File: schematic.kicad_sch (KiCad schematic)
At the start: 15 parts, among them U1 MCP6001-OT

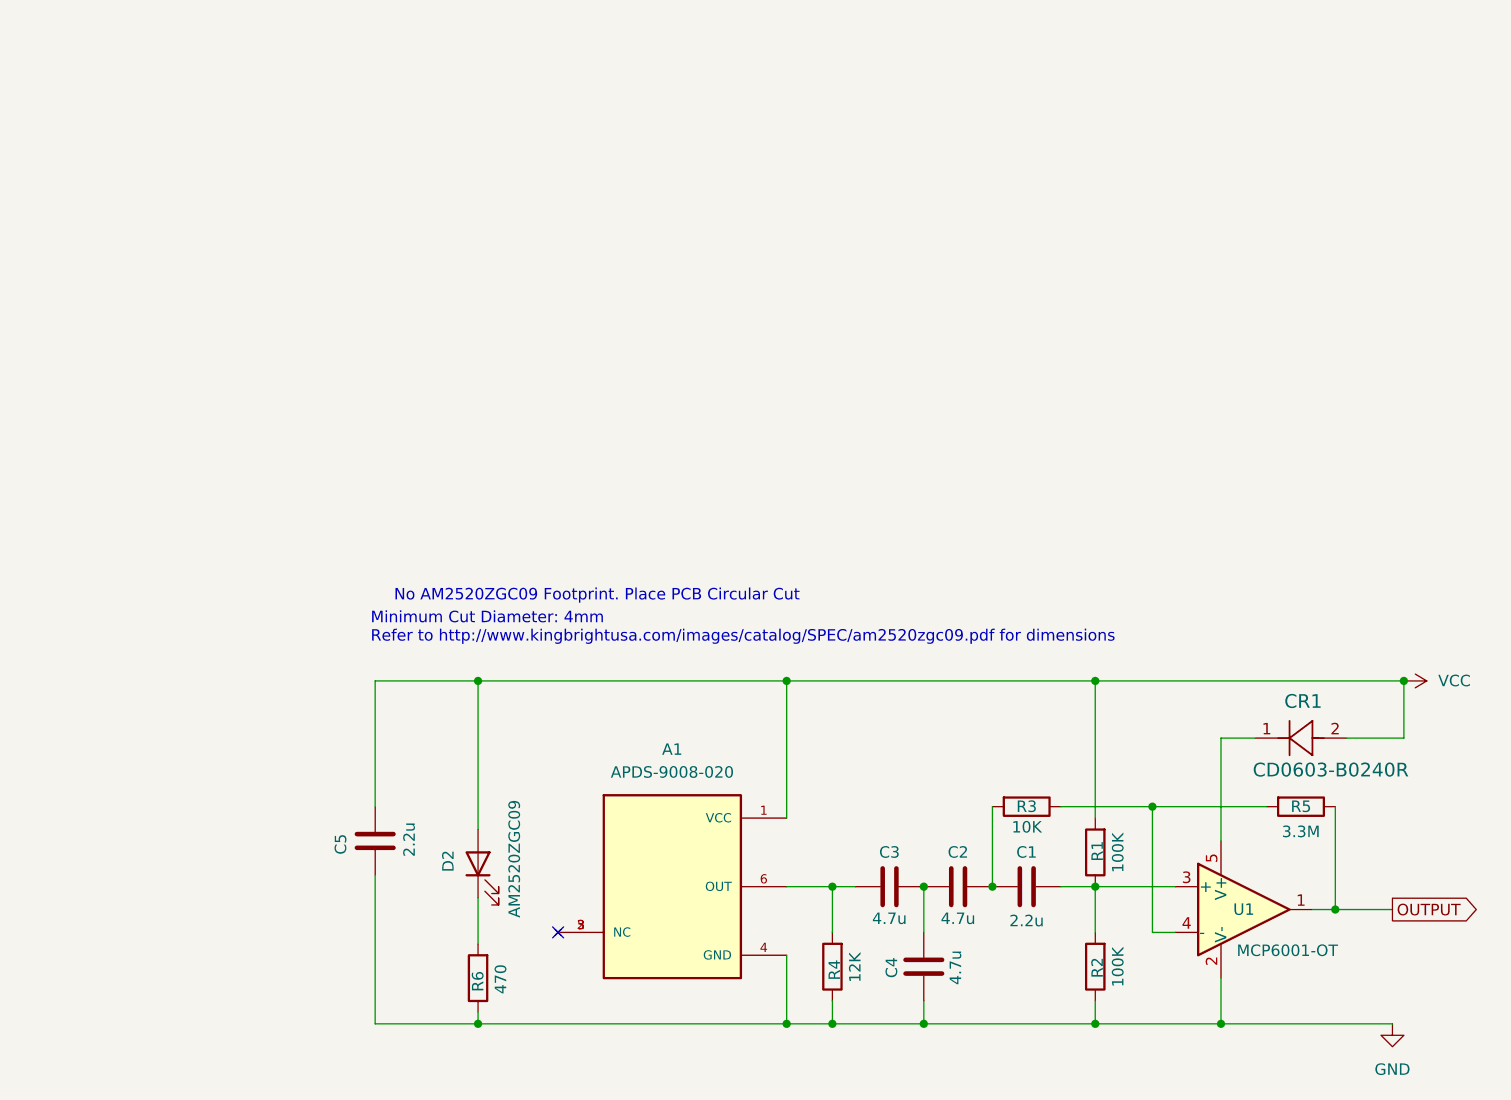
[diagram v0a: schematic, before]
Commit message: update the layout and the schematic
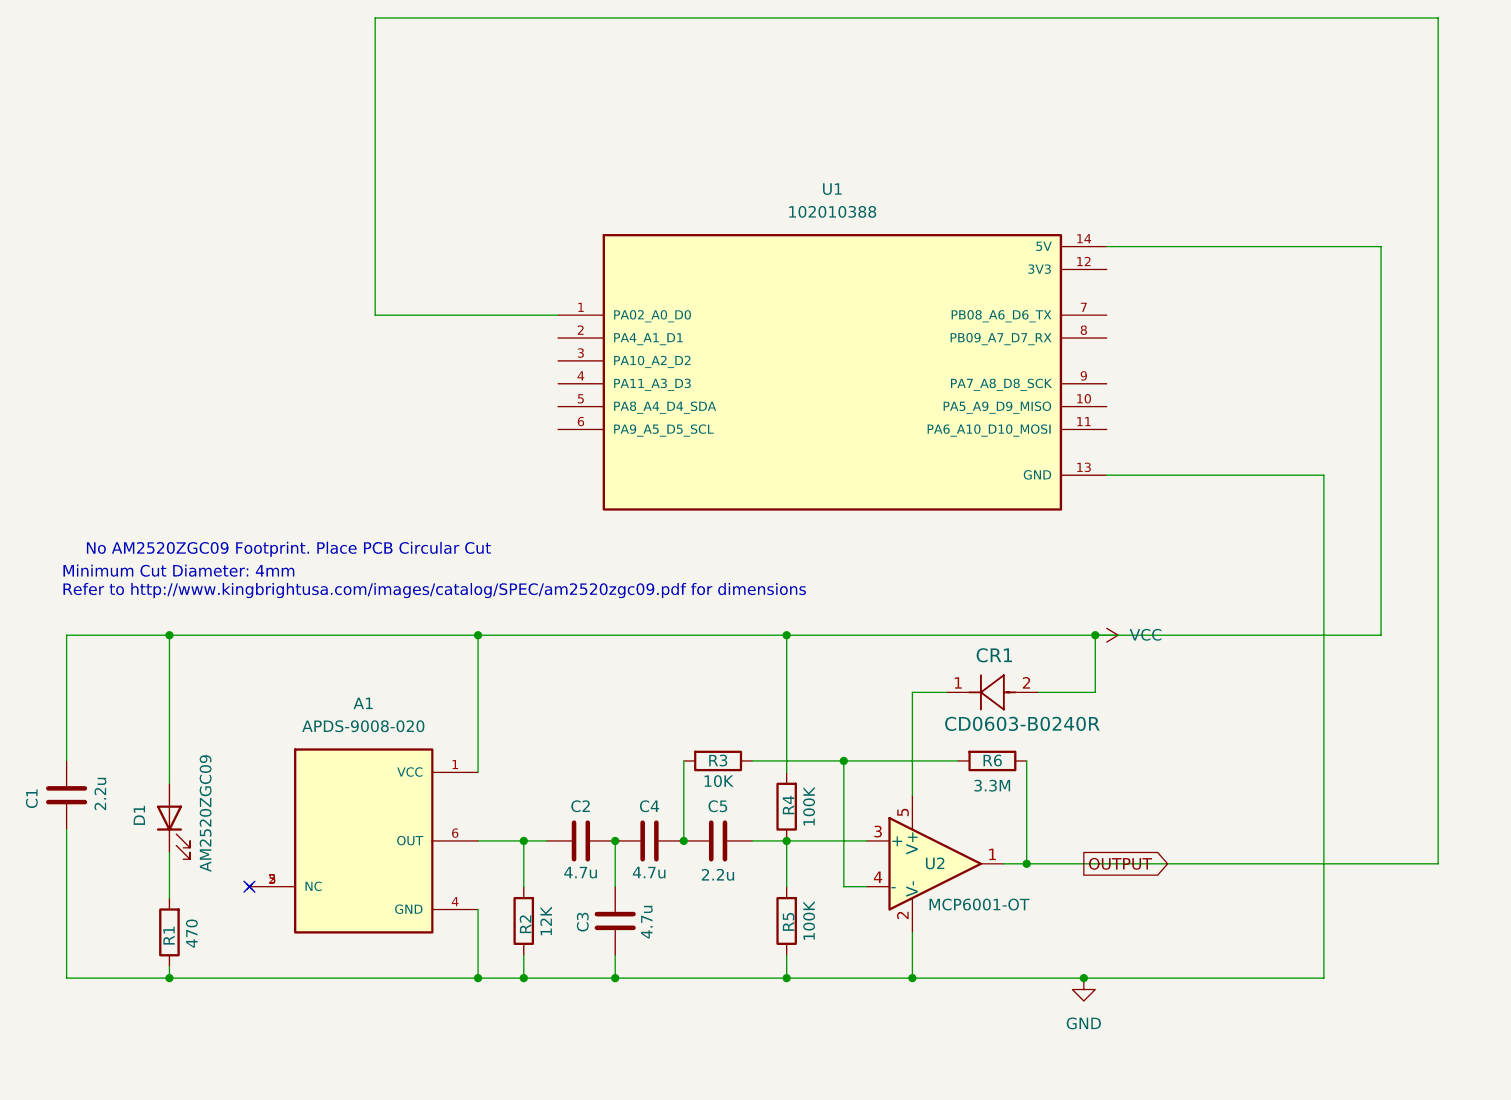
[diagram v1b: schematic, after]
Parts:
- removed D2: AM2520ZGC09, symbol Device:LED
- removed U1: MCP6001-OT, Package_TO_SOT_SMD:SOT-23-5, symbol Amplifier_Operational:MCP6001-OT
- added D1: AM2520ZGC09, LED_SMD:LED_0201_0603Metric, symbol Device:LED
- added U1: 102010388, 102010388:MODULE_102010388, symbol 102010388:102010388
- added U2: MCP6001-OT, Package_TO_SOT_SMD:HVSOF6, symbol Amplifier_Operational:MCP6001-OT
- A1: footprint (none) -> APDS-9008-020:XDCR_APDS-9008-020
- C1, C2, C3, C4, C5: footprint (none) -> Capacitor_SMD:C_0201_0603Metric_Pad0.64x0.40mm_HandSolder
- CR1: footprint DIODE_CD0603-B0240R_BRN -> footprints:DIODE_CD0603-B0240R_BRN
- R1: value 100K -> 470; footprint (none) -> Resistor_SMD:R_0201_0603Metric_Pad0.64x0.40mm_HandSolder
- R2: value 100K -> 12K; footprint (none) -> Resistor_SMD:R_0201_0603Metric_Pad0.64x0.40mm_HandSolder
- R3: footprint (none) -> Resistor_SMD:R_0201_0603Metric_Pad0.64x0.40mm_HandSolder
- R4: value 12K -> 100K; footprint (none) -> Resistor_SMD:R_0201_0603Metric_Pad0.64x0.40mm_HandSolder
- R5: value 3.3M -> 100K; footprint (none) -> Resistor_SMD:R_0201_0603Metric_Pad0.64x0.40mm_HandSolder
- R6: value 470 -> 3.3M; footprint (none) -> Resistor_SMD:R_0201_0603Metric_Pad0.64x0.40mm_HandSolder
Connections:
- net GND: now also C1.1, C3.2, R1.1, R5.1, U1.13 (GND), U2.2 (V-); no longer C4.2, C5.1, R4.1, R6.1
- net OUTPUT: now also R6.1, U1.1 (PA02_A0_D0), U2.1; no longer R5.1
- net VCC: now also C1.2, R4.2, D1.2 (A), U1.14 (5V); no longer C5.2, R1.2
- net at R5.2: now also C5.2, R4.1, U2.3 (+); no longer R3.1
- net at CR1.1: now also U2.5 (V+)
- net at R6.2: now also R3.1, U2.4 (-)
- new net: A1.6 (OUT), C2.1, R2.2
- new net: C2.2, C3.1, C4.1
- new net: D1.1 (K), R1.2
- new net: C4.2, C5.1, R3.2
